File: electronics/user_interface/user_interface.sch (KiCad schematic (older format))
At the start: 2 parts

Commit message: started with user interface schematic entry
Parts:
- added J?: Conn_01x06, symbol Connector_Generic:Conn_01x06
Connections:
- new net !INT: J?.6 (Pin_6)
- new net SCL: J?.5 (Pin_5)
- new net SDA: J?.4 (Pin_4)
- new net VDD: J?.2 (Pin_2)
- new net VDD_BACKLIGHT: J?.1 (Pin_1)
- new net VSS: J?.3 (Pin_3)
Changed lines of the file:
@@
 EESchema Schematic File Version 4
-LIBS:jlcpcb_2_layer-cache
-EELAYER 26 0
+EELAYER 30 0
 EELAYER END
 $Descr A4 11693 8268
@@
 	1    0    0    -1
 $EndComp
+$Comp
+L Connector_Generic:Conn_01x06 J?
+U 1 1 5EBB1AC4
+P 700 1000
+F 0 "J?" H 618 1417 50  0000 C CNN
+F 1 "Conn_01x06" H 618 1326 50  0000 C CNN
+F 2 "" H 700 1000 50  0001 C CNN
+F 3 "~" H 700 1000 50  0001 C CNN
+	1    700  1000
+	-1   0    0    -1
+$EndComp
+Text Label 950  1000 0    50   ~ 0
+VSS
+Text Label 950  900  0    50   ~ 0
+VDD
+Text Label 950  800  0    50   ~ 0
+VDD_BACKLIGHT
+Text Label 950  1100 0    50   ~ 0
+SDA
+Text Label 950  1200 0    50   ~ 0
+SCL
+Text Label 950  1300 0    50   ~ 0
+!INT
+Wire Wire Line
+	900  800  950  800
+Wire Wire Line
+	950  900  900  900
+Wire Wire Line
+	900  1000 950  1000
+Wire Wire Line
+	950  1100 900  1100
+Wire Wire Line
+	900  1200 950  1200
+Wire Wire Line
+	950  1300 900  1300
 $EndSCHEMATC

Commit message: power input circuit
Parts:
- added C?: 10u, SquantorRcl:C_0603, symbol Device:C
- added FB?: Ferrite_Bead_Small, SquantorRcl:L_0603, symbol Device:Ferrite_Bead_Small
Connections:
- wire segments 6 -> 10
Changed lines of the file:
@@
 Text Label 950  1000 0    50   ~ 0
 VSS
-Text Label 950  900  0    50   ~ 0
+Text Label 2050 900  0    50   ~ 0
 VDD
 Text Label 950  800  0    50   ~ 0
@@
 	900  800  950  800
 Wire Wire Line
-	950  900  900  900
-Wire Wire Line
 	900  1000 950  1000
 Wire Wire Line
@@
 Wire Wire Line
 	950  1300 900  1300
+$Comp
+L Device:Ferrite_Bead_Small FB?
+U 1 1 5EBDBD2C
+P 1500 900
+F 0 "FB?" V 1450 800 50  0000 C CNN
+F 1 "Ferrite_Bead_Small" V 1600 900 50  0000 C CNN
+F 2 "SquantorRcl:L_0603" V 1430 900 50  0001 C CNN
+F 3 "~" H 1500 900 50  0001 C CNN
+	1    1500 900
+	0    1    1    0
+$EndComp
+Wire Wire Line
+	900  900  1400 900
+Wire Wire Line
+	1600 900  2000 900
+Text Label 2000 1350 0    50   ~ 0
+VSS
+$Comp
+L Device:C C?
+U 1 1 5EBDD85D
+P 2000 1100
+F 0 "C?" H 1900 1200 50  0000 L CNN
+F 1 "10u" H 2115 1055 50  0000 L CNN
+F 2 "SquantorRcl:C_0603" H 2038 950 50  0001 C CNN
+F 3 "~" H 2000 1100 50  0001 C CNN
+	1    2000 1100
+	1    0    0    -1
+$EndComp
+Wire Wire Line
+	2000 1250 2000 1350
+Wire Wire Line
+	2000 950  2000 900
+Connection ~ 2000 900
+Wire Wire Line
+	2000 900  2050 900
 $EndSCHEMATC

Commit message: board outline, input circuit layout
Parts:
- removed C?: 10u, SquantorRcl:C_0603, symbol Device:C
- added C?: 10u, SquantorRcl:C_0805, symbol Device:C_Small
- added J?: Conn_02x05_Odd_Even, SquantorConnectors:Header-0254-2X05-H010, symbol Connector_Generic:Conn_02x05_Odd_Even
- FB1: renamed from FB?; value Ferrite_Bead_Small -> 600
- J1: renamed from J?; footprint (none) -> Connector_JST:JST_PH_S6B-PH-K_1x06_P2.00mm_Horizontal
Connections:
- net labels added: VDD_RAW
- wire segments 10 -> 28
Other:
- moved on the sheet: FB1, J1
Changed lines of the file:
@@
 $EndComp
 $Comp
-L Connector_Generic:Conn_01x06 J?
+L Connector_Generic:Conn_01x06 J1
 U 1 1 5EBB1AC4
-P 700 1000
-F 0 "J?" H 618 1417 50  0000 C CNN
-F 1 "Conn_01x06" H 618 1326 50  0000 C CNN
-F 2 "" H 700 1000 50  0001 C CNN
-F 3 "~" H 700 1000 50  0001 C CNN
-	1    700  1000
+P 750 850
+F 0 "J1" H 750 1150 50  0000 C CNN
+F 1 "Conn_01x06" H 750 450 50  0000 C CNN
+F 2 "Connector_JST:JST_PH_S6B-PH-K_1x06_P2.00mm_Horizontal" H 750 850 50  0001 C CNN
+F 3 "~" H 750 850 50  0001 C CNN
+	1    750  850
 	-1   0    0    -1
 $EndComp
-Text Label 950  1000 0    50   ~ 0
+Text Label 1000 850  0    50   ~ 0
 VSS
-Text Label 2050 900  0    50   ~ 0
+Text Label 3000 950  0    50   ~ 0
 VDD
-Text Label 950  800  0    50   ~ 0
+Text Label 1000 650  0    50   ~ 0
 VDD_BACKLIGHT
-Text Label 950  1100 0    50   ~ 0
+Text Label 1000 950  0    50   ~ 0
 SDA
-Text Label 950  1200 0    50   ~ 0
+Text Label 1000 1050 0    50   ~ 0
 SCL
-Text Label 950  1300 0    50   ~ 0
+Text Label 1000 1150 0    50   ~ 0
 !INT
 Wire Wire Line
-	900  800  950  800
+	950  650  1000 650
 Wire Wire Line
-	900  1000 950  1000
+	950  850  1000 850
 Wire Wire Line
-	950  1100 900  1100
+	1000 950  950  950
 Wire Wire Line
-	900  1200 950  1200
+	950  1050 1000 1050
 Wire Wire Line
-	950  1300 900  1300
+	1000 1150 950  1150
 $Comp
-L Device:Ferrite_Bead_Small FB?
+L Device:Ferrite_Bead_Small FB1
 U 1 1 5EBDBD2C
-P 1500 900
-F 0 "FB?" V 1450 800 50  0000 C CNN
-F 1 "Ferrite_Bead_Small" V 1600 900 50  0000 C CNN
-F 2 "SquantorRcl:L_0603" V 1430 900 50  0001 C CNN
-F 3 "~" H 1500 900 50  0001 C CNN
-	1    1500 900
+P 2750 950
+F 0 "FB1" V 2700 850 50  0000 C CNN
+F 1 "600" V 2800 1050 50  0000 C CNN
+F 2 "SquantorRcl:L_0603" V 2680 950 50  0001 C CNN
+F 3 "~" H 2750 950 50  0001 C CNN
+	1    2750 950
+	0    1    1    0
+$EndComp
+Text Label 2550 1150 2    50   ~ 0
+VSS
+Wire Wire Line
+	2650 1150 2550 1150
+$Comp
+L Connector_Generic:Conn_02x05_Odd_Even J?
+U 1 1 5EBE0632
+P 1050 1700
+F 0 "J?" H 1100 2000 50  0000 C CNN
+F 1 "Conn_02x05_Odd_Even" H 1050 1400 50  0000 C CNN
+F 2 "SquantorConnectors:Header-0254-2X05-H010" H 1050 1700 50  0001 C CNN
+F 3 "~" H 1050 1700 50  0001 C CNN
+	1    1050 1700
+	1    0    0    -1
+$EndComp
+Text Label 850  2150 0    50   ~ 0
+VSS
+Wire Wire Line
+	850  1500 800  1500
+Wire Wire Line
+	800  1500 800  1600
+Wire Wire Line
+	800  2150 850  2150
+Wire Wire Line
+	850  1900 800  1900
+Connection ~ 800  1900
+Wire Wire Line
+	800  1900 800  2150
+Wire Wire Line
+	850  1800 800  1800
+Connection ~ 800  1800
+Wire Wire Line
+	800  1800 800  1900
+Wire Wire Line
+	850  1700 800  1700
+Connection ~ 800  1700
+Wire Wire Line
+	800  1700 800  1800
+Wire Wire Line
+	850  1600 800  1600
+Connection ~ 800  1600
+Wire Wire Line
+	800  1600 800  1700
+Text Label 1400 1500 0    50   ~ 0
+VDD_BACKLIGHT
+Wire Wire Line
+	950  750  1000 750
+Text Label 1000 750  0    50   ~ 0
+VDD_RAW
+Text Label 1400 1600 0    50   ~ 0
+VDD_RAW
+Text Label 1400 1700 0    50   ~ 0
+SDA
+Text Label 1400 1800 0    50   ~ 0
+SCL
+Text Label 1400 1900 0    50   ~ 0
+!INT
+Wire Wire Line
+	1350 1500 1400 1500
+Wire Wire Line
+	1400 1600 1350 1600
+Wire Wire Line
+	1350 1700 1400 1700
+Wire Wire Line
+	1400 1800 1350 1800
+Wire Wire Line
+	1350 1900 1400 1900
+Text Label 2550 950  2    50   ~ 0
+VDD_RAW
+Wire Wire Line
+	2650 950  2550 950
+Wire Wire Line
+	2850 950  2950 950
+$Comp
+L Device:C_Small C?
+U 1 1 5EBF6E62
+P 2750 1150
+F 0 "C?" V 2700 1050 50  0000 C CNN
+F 1 "10u" V 2800 1250 50  0000 C CNN
+F 2 "SquantorRcl:C_0805" H 2750 1150 50  0001 C CNN
+F 3 "~" H 2750 1150 50  0001 C CNN
+	1    2750 1150
 	0    1    1    0
 $EndComp
 Wire Wire Line
-	900  900  1400 900
+	2850 1150 2950 1150
 Wire Wire Line
-	1600 900  2000 900
-Text Label 2000 1350 0    50   ~ 0
-VSS
-$Comp
-L Device:C C?
-U 1 1 5EBDD85D
-P 2000 1100
-F 0 "C?" H 1900 1200 50  0000 L CNN
-F 1 "10u" H 2115 1055 50  0000 L CNN
-F 2 "SquantorRcl:C_0603" H 2038 950 50  0001 C CNN
-F 3 "~" H 2000 1100 50  0001 C CNN
-	1    2000 1100
-	1    0    0    -1
-$EndComp
+	2950 1150 2950 950
+Connection ~ 2950 950
 Wire Wire Line
-	2000 1250 2000 1350
-Wire Wire Line
-	2000 950  2000 900
-Connection ~ 2000 900
-Wire Wire Line
-	2000 900  2050 900
+	2950 950  3000 950
 $EndSCHEMATC

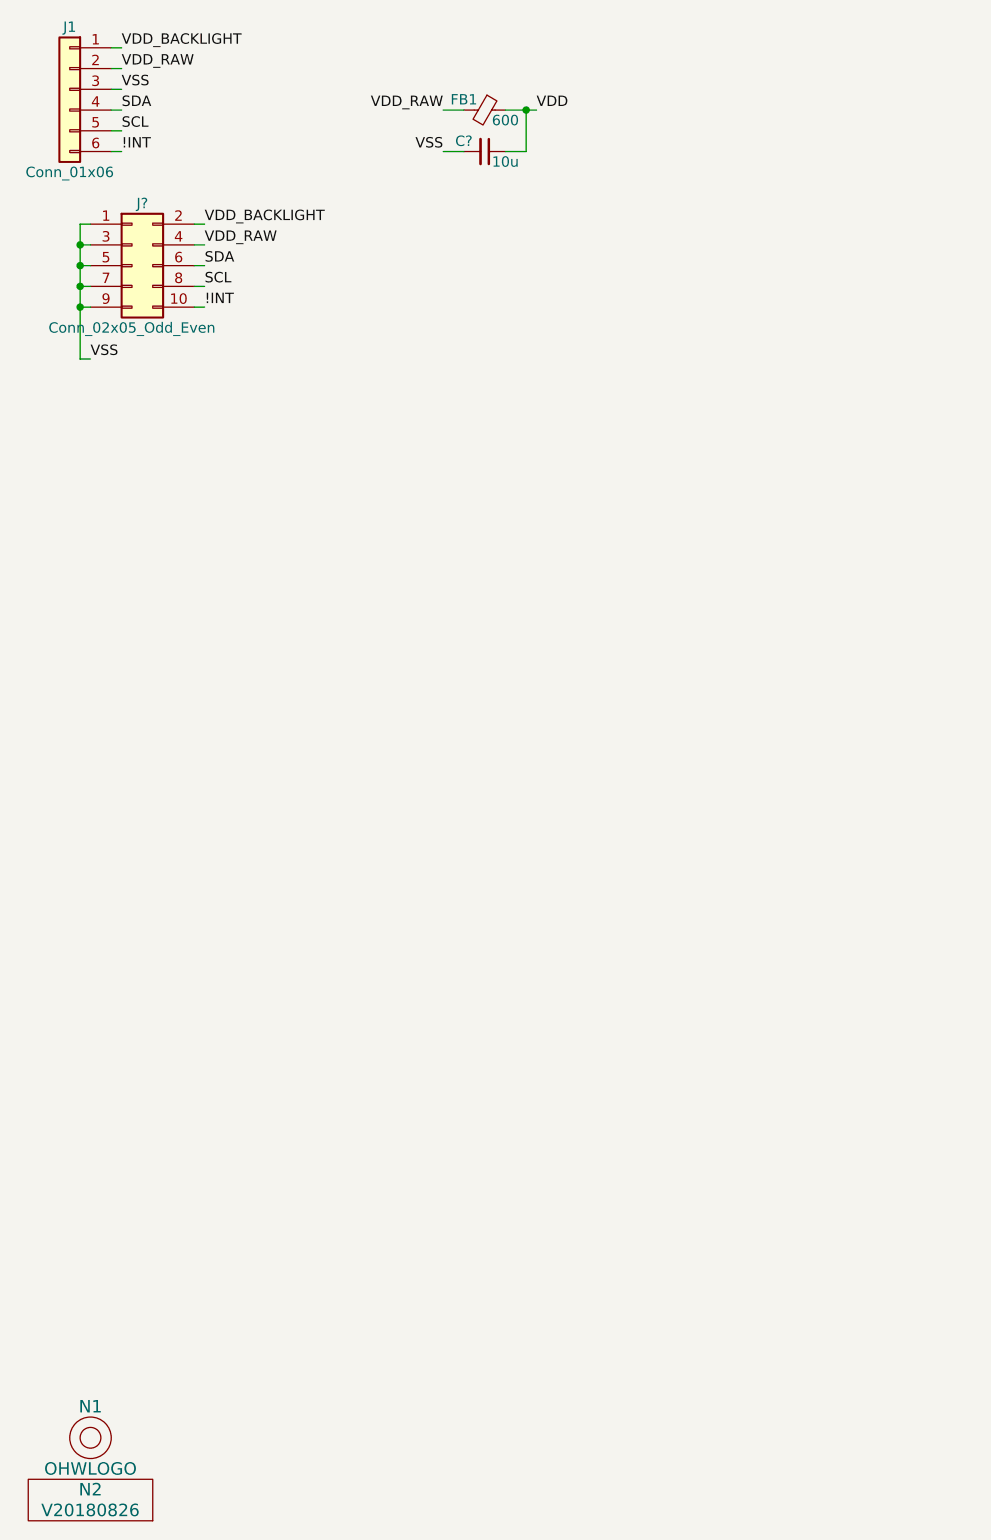
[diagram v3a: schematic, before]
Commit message: footprints assignment, minor layout positioning
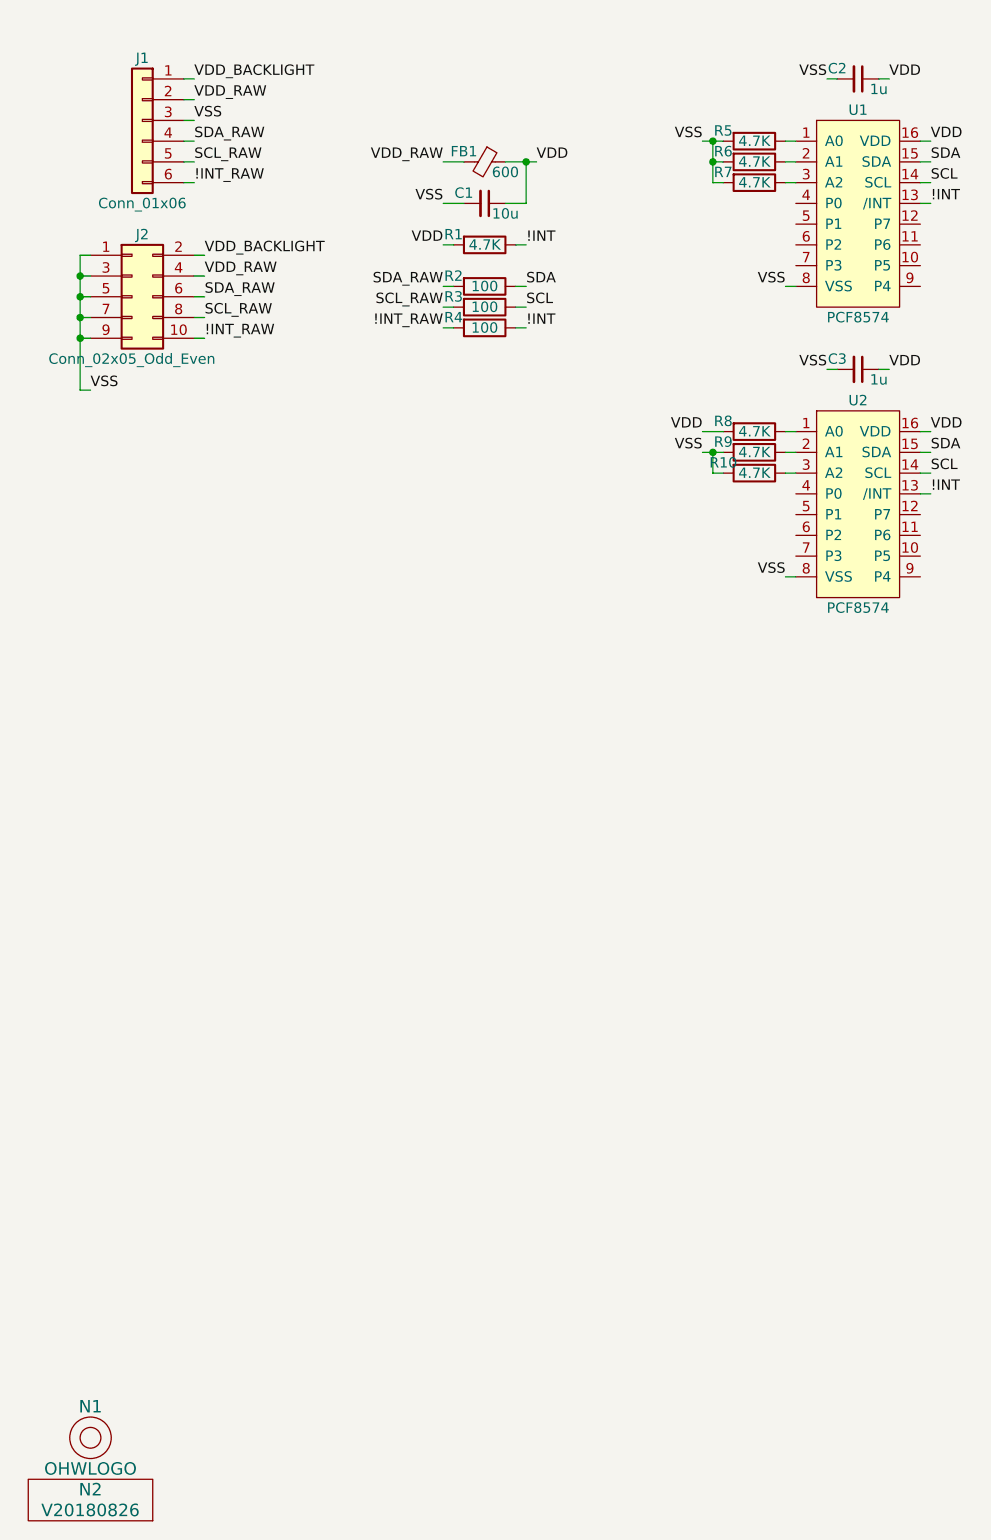
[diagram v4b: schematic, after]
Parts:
- added C2, C3: 1u, SquantorRcl:C_0603, symbol Device:C_Small
- added R1, R10, R5, R6, R7, R8, R9: 4.7K, SquantorRcl:R_0603_hand, symbol Device:R
- added R2, R3, R4: 100, SquantorRcl:R_0603_hand, symbol Device:R
- added U1, U2: PCF8574, SquantorIC:SOT162-1-NXP, symbol SquantorNxp:PCF8574
- C1: renamed from C?; footprint SquantorRcl:C_0805 -> SquantorRcl:C_0603
- gave numbers to parts that had none: 1
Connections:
- net !INT: now also R1.1, R4.1, U1.13 (/INT), U2.13 (/INT); no longer J1.6 (Pin_6), J2.10 (Pin_10)
- net SCL: now also R3.1, U1.14 (SCL), U2.14 (SCL); no longer J1.5 (Pin_5), J2.8 (Pin_8)
- net SDA: now also R2.1, U1.15 (SDA), U2.15 (SDA); no longer J1.4 (Pin_4), J2.6 (Pin_6)
- net VDD: now also C2.1, C3.1, R1.2, R8.2, U1.16 (VDD), U2.16 (VDD)
- net VSS: now also C2.2, C3.2, R10.2, R5.2, R6.2, R7.2, R9.2, U1.8 (VSS), U2.8 (VSS)
- new net: R5.1, U1.1 (A0)
- new net: R6.1, U1.2 (A1)
- new net: R7.1, U1.3 (A2)
- new net: R8.1, U2.1 (A0)
- new net: R9.1, U2.2 (A1)
- new net: R10.1, U2.3 (A2)
- new net !INT_RAW: J1.6 (Pin_6), J2.10 (Pin_10), R4.2
- new net SCL_RAW: J1.5 (Pin_5), J2.8 (Pin_8), R3.2
- new net SDA_RAW: J1.4 (Pin_4), J2.6 (Pin_6), R2.2
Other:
- moved on the sheet: C1, FB1, J1, J2

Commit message: updated date
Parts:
- N2: value V20180826 -> V20200514
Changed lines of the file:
@@
 P 850 7700
 F 0 "N2" H 850 7800 60  0000 C CNN
-F 1 "V20180826" H 850 7700 60  0000 C CNN
+F 1 "V20200514" H 850 7700 60  0000 C CNN
 F 2 "SquantorLabels:Label_version" H 850 7700 60  0001 C CNN
 F 3 "" H 850 7700 60  0001 C CNN

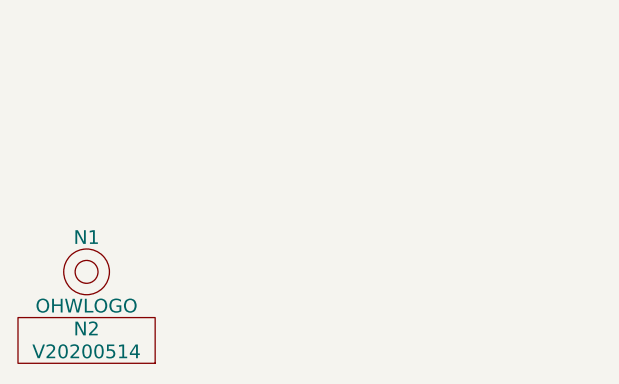
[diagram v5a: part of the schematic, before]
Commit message: added mounting holes, some silk moves
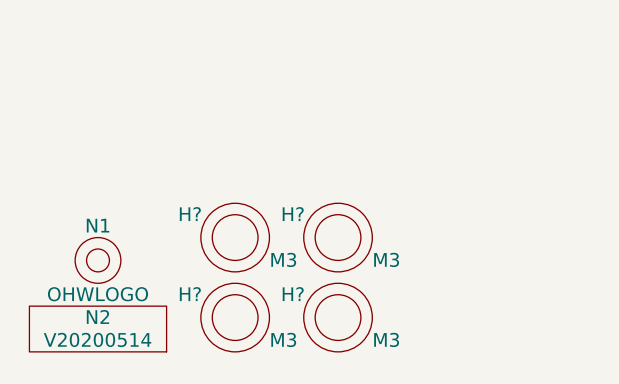
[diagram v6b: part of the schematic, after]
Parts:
- added H? (x4): M3, MountingHole:MountingHole_3.2mm_M3_Pad_Via, symbol SquantorPCBOutline:Drill_Hole_no_metal
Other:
- moved on the sheet: N1, N2
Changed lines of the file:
@@
 L SquantorLabels:VYYYYMMDD N2
 U 1 1 5A1357A5
-P 850 7700
-F 0 "N2" H 850 7800 60  0000 C CNN
-F 1 "V20200514" H 850 7700 60  0000 C CNN
-F 2 "SquantorLabels:Label_version" H 850 7700 60  0001 C CNN
-F 3 "" H 850 7700 60  0001 C CNN
-	1    850  7700
+P 900 7650
+F 0 "N2" H 900 7750 60  0000 C CNN
+F 1 "V20200514" H 900 7650 60  0000 C CNN
+F 2 "SquantorLabels:Label_version" H 900 7650 60  0001 C CNN
+F 3 "" H 900 7650 60  0001 C CNN
+	1    900  7650
 	1    0    0    -1
 $EndComp
@@
 L SquantorLabels:OHWLOGO N1
 U 1 1 5A135869
-P 850 7350
-F 0 "N1" H 850 7500 60  0000 C CNN
-F 1 "OHWLOGO" H 850 7200 60  0000 C CNN
-F 2 "Symbols:OSHW-Symbol_6.7x6mm_SilkScreen" H 850 7350 60  0001 C CNN
-F 3 "" H 850 7350 60  0001 C CNN
-	1    850  7350
+P 900 7300
+F 0 "N1" H 900 7450 60  0000 C CNN
+F 1 "OHWLOGO" H 900 7150 60  0000 C CNN
+F 2 "Symbols:OSHW-Symbol_6.7x6mm_SilkScreen" H 900 7300 60  0001 C CNN
+F 3 "" H 900 7300 60  0001 C CNN
+	1    900  7300
 	1    0    0    -1
 $EndComp
@@
 Wire Wire Line
 	3800 2500 3900 2500
+$Comp
+L SquantorPCBOutline:Drill_Hole_no_metal H?
+U 1 1 5EBF62F7
+P 1500 7550
+F 0 "H?" H 1250 7650 60  0000 L CNN
+F 1 "M3" H 1650 7450 60  0000 L CNN
+F 2 "MountingHole:MountingHole_3.2mm_M3_Pad_Via" H 1500 7550 60  0001 C CNN
+F 3 "" H 1500 7550 60  0001 C CNN
+	1    1500 7550
+	1    0    0    -1
+$EndComp
+$Comp
+L SquantorPCBOutline:Drill_Hole_no_metal H?
+U 1 1 5EBF718B
+P 1500 7200
+F 0 "H?" H 1250 7300 60  0000 L CNN
+F 1 "M3" H 1650 7100 60  0000 L CNN
+F 2 "MountingHole:MountingHole_3.2mm_M3_Pad_Via" H 1500 7200 60  0001 C CNN
+F 3 "" H 1500 7200 60  0001 C CNN
+	1    1500 7200
+	1    0    0    -1
+$EndComp
+$Comp
+L SquantorPCBOutline:Drill_Hole_no_metal H?
+U 1 1 5EBF7413
+P 1950 7200
+F 0 "H?" H 1700 7300 60  0000 L CNN
+F 1 "M3" H 2100 7100 60  0000 L CNN
+F 2 "MountingHole:MountingHole_3.2mm_M3_Pad_Via" H 1950 7200 60  0001 C CNN
+F 3 "" H 1950 7200 60  0001 C CNN
+	1    1950 7200
+	1    0    0    -1
+$EndComp
+$Comp
+L SquantorPCBOutline:Drill_Hole_no_metal H?
+U 1 1 5EBF8235
+P 1950 7550
+F 0 "H?" H 1700 7650 60  0000 L CNN
+F 1 "M3" H 2100 7450 60  0000 L CNN
+F 2 "MountingHole:MountingHole_3.2mm_M3_Pad_Via" H 1950 7550 60  0001 C CNN
+F 3 "" H 1950 7550 60  0001 C CNN
+	1    1950 7550
+	1    0    0    -1
+$EndComp
 $EndSCHEMATC

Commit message: minor schematic updates
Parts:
- gave numbers to parts that had none: 4
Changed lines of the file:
@@
 	3800 2500 3900 2500
 $Comp
-L SquantorPCBOutline:Drill_Hole_no_metal H?
+L SquantorPCBOutline:Drill_Hole_no_metal H2
 U 1 1 5EBF62F7
 P 1500 7550
-F 0 "H?" H 1250 7650 60  0000 L CNN
+F 0 "H2" H 1250 7650 60  0000 L CNN
 F 1 "M3" H 1650 7450 60  0000 L CNN
 F 2 "MountingHole:MountingHole_3.2mm_M3_Pad_Via" H 1500 7550 60  0001 C CNN
@@
 $EndComp
 $Comp
-L SquantorPCBOutline:Drill_Hole_no_metal H?
+L SquantorPCBOutline:Drill_Hole_no_metal H1
 U 1 1 5EBF718B
 P 1500 7200
-F 0 "H?" H 1250 7300 60  0000 L CNN
+F 0 "H1" H 1250 7300 60  0000 L CNN
 F 1 "M3" H 1650 7100 60  0000 L CNN
 F 2 "MountingHole:MountingHole_3.2mm_M3_Pad_Via" H 1500 7200 60  0001 C CNN
@@
 $EndComp
 $Comp
-L SquantorPCBOutline:Drill_Hole_no_metal H?
+L SquantorPCBOutline:Drill_Hole_no_metal H3
 U 1 1 5EBF7413
 P 1950 7200
-F 0 "H?" H 1700 7300 60  0000 L CNN
+F 0 "H3" H 1700 7300 60  0000 L CNN
 F 1 "M3" H 2100 7100 60  0000 L CNN
 F 2 "MountingHole:MountingHole_3.2mm_M3_Pad_Via" H 1950 7200 60  0001 C CNN
@@
 $EndComp
 $Comp
-L SquantorPCBOutline:Drill_Hole_no_metal H?
+L SquantorPCBOutline:Drill_Hole_no_metal H4
 U 1 1 5EBF8235
 P 1950 7550
-F 0 "H?" H 1700 7650 60  0000 L CNN
+F 0 "H4" H 1700 7650 60  0000 L CNN
 F 1 "M3" H 2100 7450 60  0000 L CNN
 F 2 "MountingHole:MountingHole_3.2mm_M3_Pad_Via" H 1950 7550 60  0001 C CNN
